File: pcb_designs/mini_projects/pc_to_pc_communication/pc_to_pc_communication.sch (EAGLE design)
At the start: 14 parts, among them IC1 MAX232, IC2 74S51N, T1 SL100, T2 SL100, X1 DB 9 FEMALE

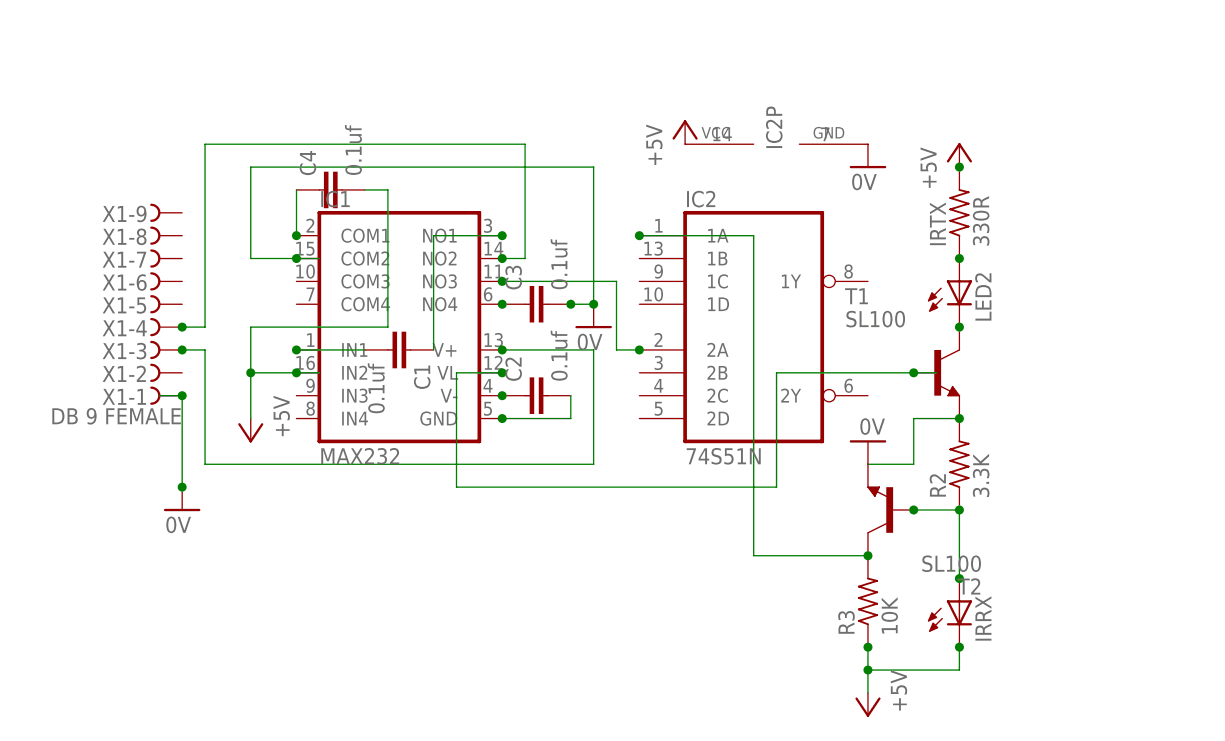
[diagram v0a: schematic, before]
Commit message: 
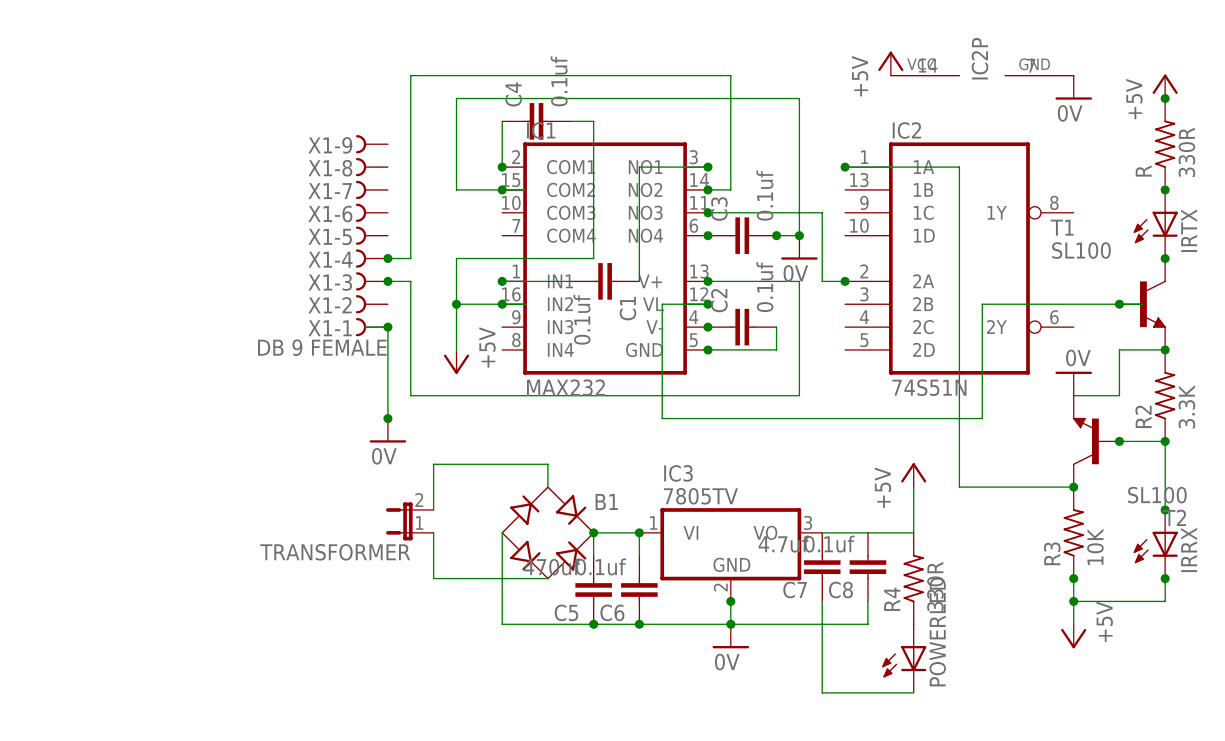
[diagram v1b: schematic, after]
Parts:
- removed LED2: (no value), led:LED3MM
- added B1: (no value), rectifier:B-DIL
- added C5: 470uf, capacitor-wima:C2,5-3
- added C6, C8: 0.1uf, capacitor-wima:C2,5-3
- added C7: 4.7uf, capacitor-wima:C2,5-3
- added IC3: 7805TV, linear:7805TV
- added POWERLED: (no value), led:LED3MM
- added R, R4: 330R, resistor:R-US_0204/7
- added TRANSFORMER: (no value), jumper:JP1E
- IRTX: value 330R -> (none); device resistor:R-US_0204/7 -> led:LED3MM
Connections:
- new net N$16: B1.+, C5.2, C6.2, IC3.VI
- new net N$17: B1.AC1, TRANSFORMER.2
- new net N$18: B1.AC2, TRANSFORMER.1
- new net N$21: POWERLED.A, R4.1
- net +5V: now also C7.2, C8.2, IC3.VO, R.2, R4.2; no longer IRTX.2
- net 0V: now also B1.-, C5.1, C6.1, C7.1, C8.1, IC3.GND, POWERLED.C
- net N$6: now also IRTX.C; no longer LED2.C
- net N$8: now also IRTX.A, R.1; no longer IRTX.1, LED2.A
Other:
- moved on the sheet: C1, C2, C3, C4, IC1, IC2, IC2P, IRRX, R2, R3, T1, T2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
